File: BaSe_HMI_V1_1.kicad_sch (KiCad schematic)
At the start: 25 parts

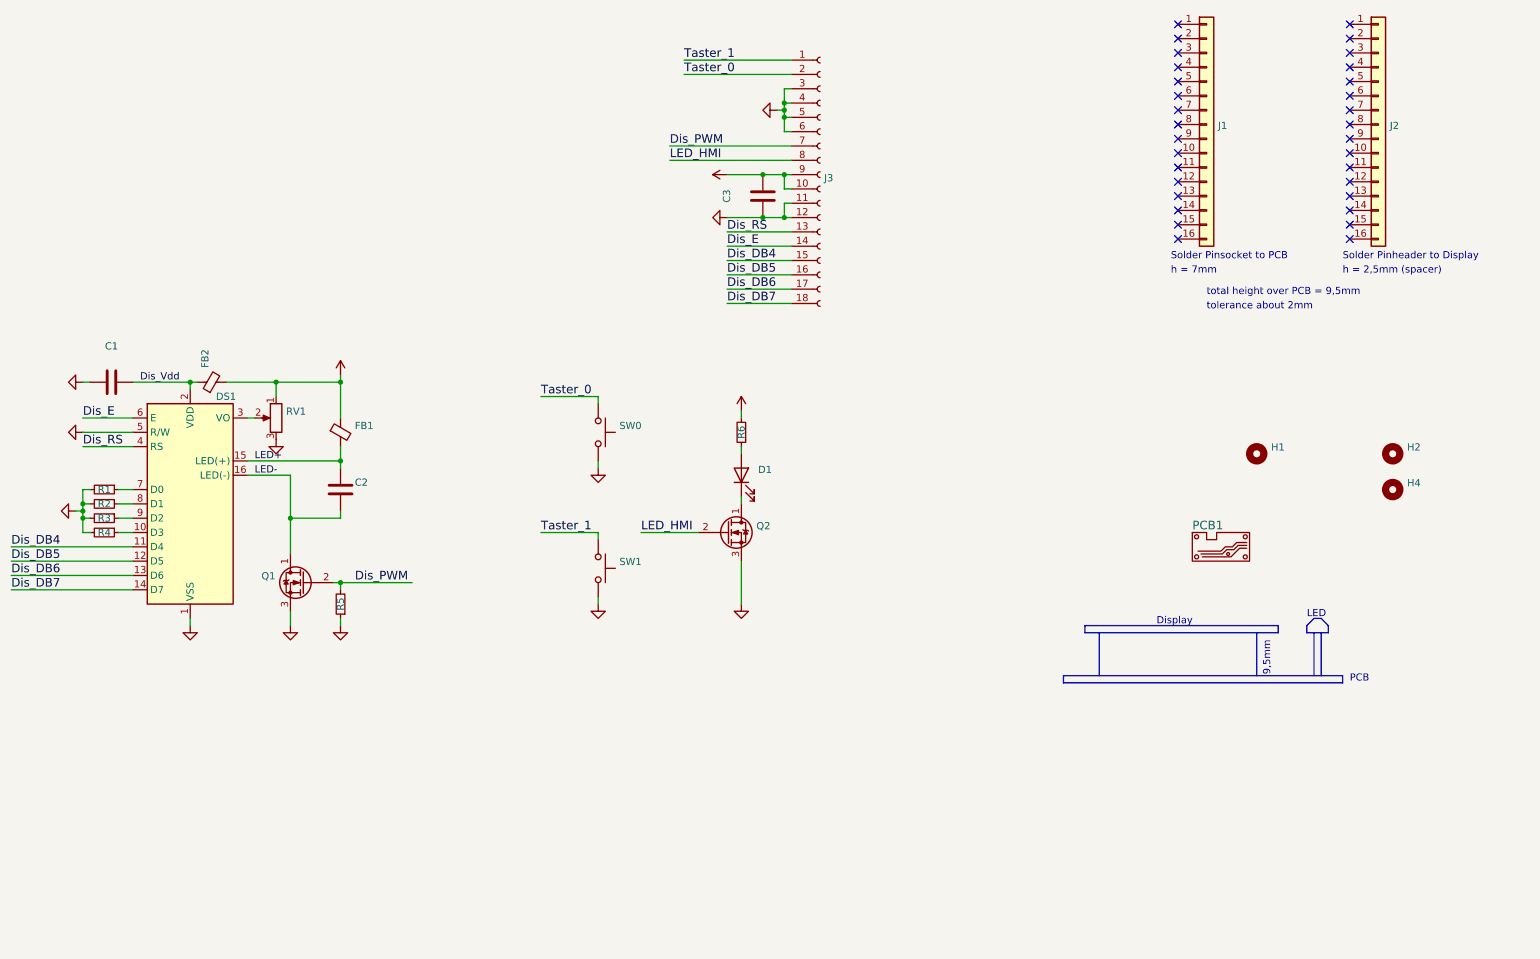
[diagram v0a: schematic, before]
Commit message: v1.1 manufactured by jlcpcb
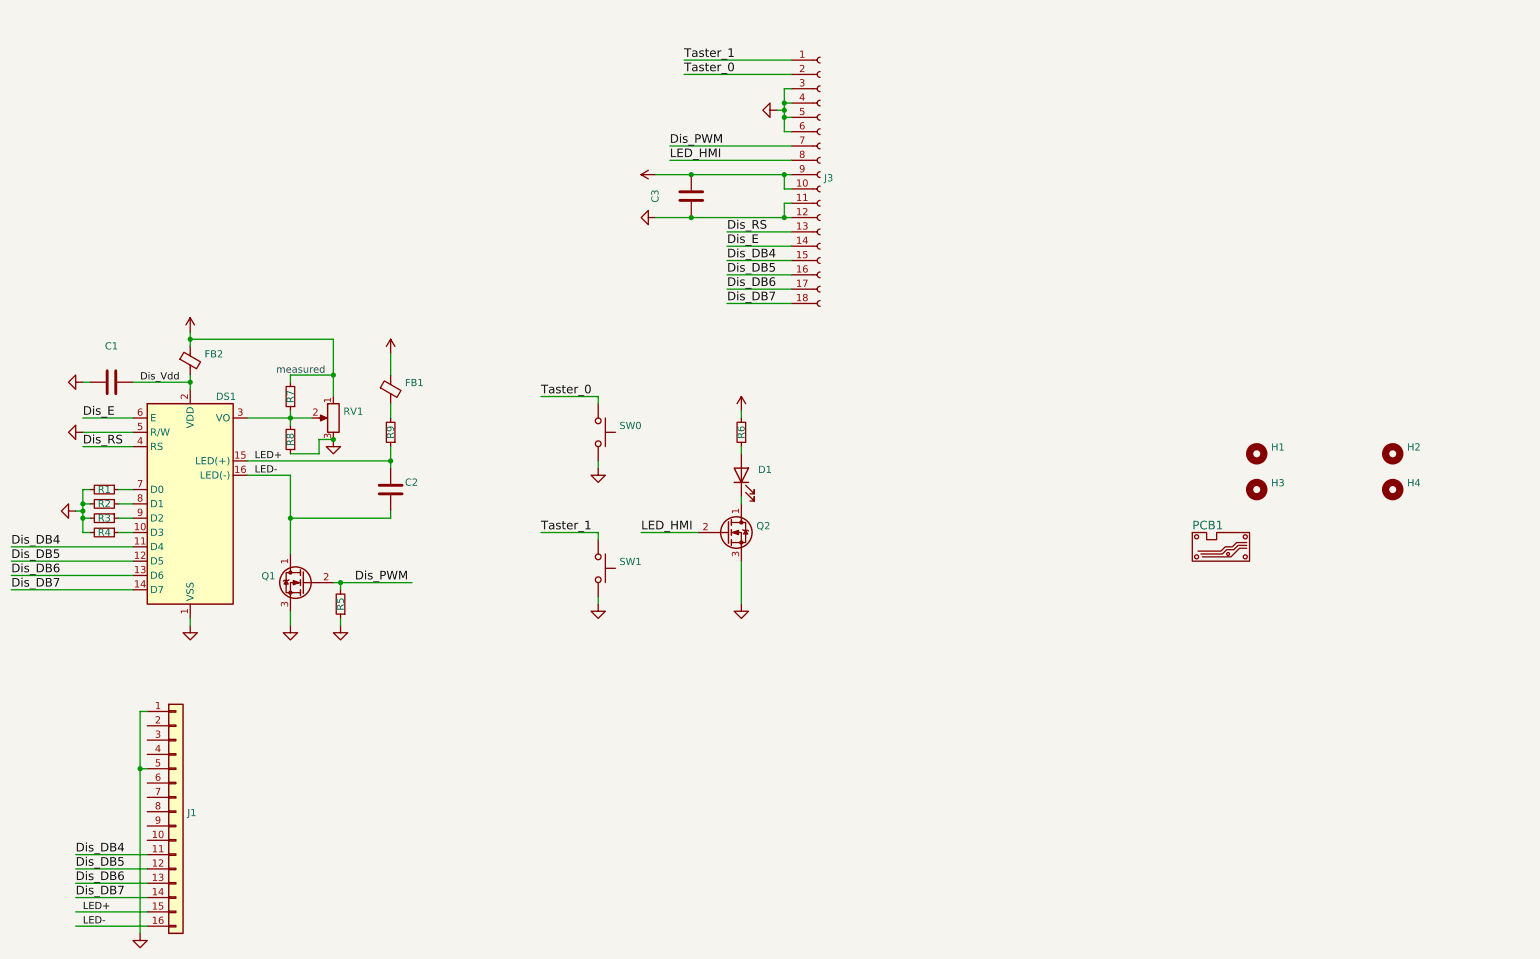
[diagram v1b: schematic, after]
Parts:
- removed J2: (no value), symbol Connector_Generic:Conn_01x16
- added H3: (no value), symbol Mechanical:MountingHole
- added R7, R8, R9: (no value), symbol Device:R_Small
- C1, C3: SPN (none) -> 311-1779-1-ND
- C2: SPN 587-1387-1-ND -> 587-1387-1-ND
- D1: SPN (none) -> C5SMF-RJF-CT0W0BB2CT-ND
- FB1, FB2: SPN (none) -> 732-4660-1-ND
- J1: Digikey 1212-1202-ND -> (none); SPN 1212-1202-ND -> 2057-PH1-16-UA-ND
- Q1, Q2: SPN (none) -> BS170-D75ZCT-ND
- R5: SPN (none) -> 311-10.0KHRCT-ND
- R6: SPN (none) -> A129673CT-ND
- SW1: SPN (none) -> 486-3459-ND
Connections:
- net +5V: now also FB2.1, R7.2; no longer FB2.2
- net Dis_DB4: now also J1.11 (Pin_11)
- net Dis_DB5: now also J1.12 (Pin_12)
- net Dis_DB6: now also J1.13 (Pin_13)
- net Dis_DB7: now also J1.14 (Pin_14)
- net Dis_Vdd: now also FB2.2; no longer FB2.1
- net GND: now also J1.1 (Pin_1), J1.5 (Pin_5), R8.1
- net LED+: now also J1.15 (Pin_15), R9.1; no longer FB1.2
- net LED-: now also J1.16 (Pin_16)
- net at DS1.3 (VO), RV1.2: now also R7.1, R8.2
- new net: FB1.2, R9.2
- no-connect marks 32 -> 0
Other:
- note added: "measured"
- note removed: "9,5mm"
- note removed: "Display"
- note removed: "LED"
- note removed: "PCB"
- note removed: "Solder Pinheader to Display"
- note removed: "Solder Pinsocket to PCB"
- note removed: "h = 2,5mm (spacer)"
- note removed: "h = 7mm"
- note removed: "tolerance about 2mm"
- note removed: "total height over PCB = 9,5mm"
- title: BaSe_HMI_V1_0 -> BaSe_HMI_V1_1
- moved on the sheet: C2, C3, FB1, FB2, RV1
